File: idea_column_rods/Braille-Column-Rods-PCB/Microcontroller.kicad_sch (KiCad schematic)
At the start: 12 parts, among them J2 Conn_01x02, J3 Conn_01x02, J4 Conn_01x08, SW1 SW_Push, SW2 SW_Push, U3 RP2040-Zero

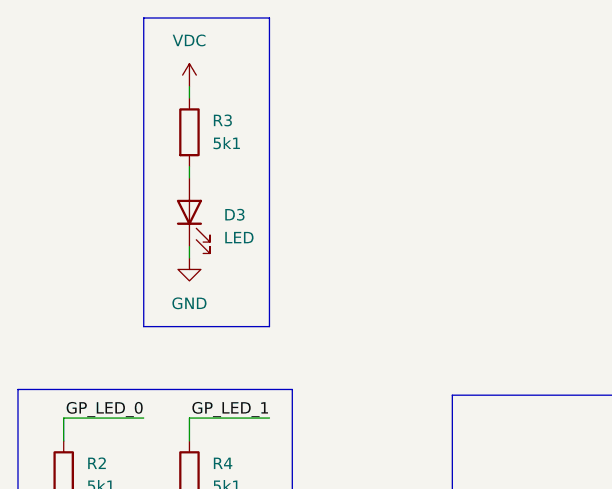
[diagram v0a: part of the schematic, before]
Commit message: WIP: Place the housing and motor X
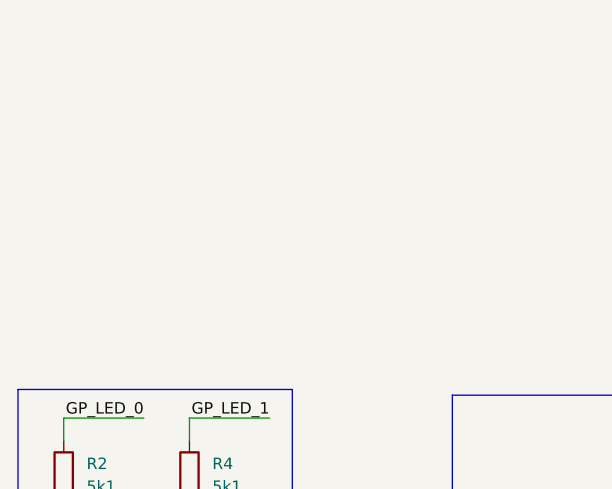
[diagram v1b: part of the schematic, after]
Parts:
- removed D3: LED, LED_SMD:LED_0603_1608Metric_Pad1.05x0.95mm_HandSolder, symbol Device:LED
- removed R3: 5k1, Resistor_SMD:R_0603_1608Metric_Pad0.98x0.95mm_HandSolder, symbol Device:R

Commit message: WIP: Manual routing and silkscreens
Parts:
- removed J2: Conn_01x02, Connector_PinHeader_2.54mm:PinHeader_1x02_P2.54mm_Vertical, symbol Connector_Generic:Conn_01x02
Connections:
- net I2C_SCL: now reaches U3.8 (GP15)
- net I2C_SDA: now reaches U3.9 (GP14)
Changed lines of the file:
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@@
+		)
+	)
+	(global_label "I2C_SDA"
+		(shape input)
+		(at 86.36 91.44 180)
+		(fields_autoplaced yes)
+		(effects
+			(font
+				(size 1.27 1.27)
+			)
+			(justify right)
+		)
+		(property "Intersheetrefs" "${INTERSHEET_REFS}"
+			(at 75.7548 91.44 0)
+			(effects
+				(font
+					(size 1.27 1.27)
+				)
+				(justify right)
+				(hide yes)
+			)
+		)
+	)
+	(global_label "I2C_SCL"
+		(shape input)
+		(at 86.36 88.9 180)
+		(fields_autoplaced yes)
+		(effects
+			(font
+				(size 1.27 1.27)
+			)
+			(justify right)
+		)
+		(property "Intersheetrefs" "${INTERSHEET_REFS}"
+			(at 75.8153 88.9 0)
+			(effects
+				(font
+					(size 1.27 1.27)
+				)
+				(justify right)
+				(hide yes)
+			)
 		)
 	)
@@
 					(unit 1)
 				)
-			)
-		)
-	)
-	(symbol
-		(lib_id "Connector_Generic:Conn_01x02")
-		(at 81.28 88.9 0)
-		(mirror y)
-		(unit 1)
-		(exclude_from_sim no)
-		(in_bom yes)
-		(on_board yes)
-		(dnp no)
-		(property "Reference" "J2"
-			(at 78.994 90.17 90)
-			(effects
-				(font
-					(size 1.27 1.27)
-				)
-			)
-		)
-		(property "Value" "Conn_01x02"
-			(at 81.28 85.09 0)
-			(effects
-				(font
-					(size 1.27 1.27)
-				)
-				(hide yes)
-			)
-		)
-		(property "Footprint" "Connector_PinHeader_2.54mm:PinHeader_1x02_P2.54mm_Vertical"
-			(at 81.28 88.9 0)
-			(effects
-				(font
-					(size 1.27 1.27)
-				)
-				(hide yes)
-			)
-		)
-		(property "Datasheet" "~"
-			(at 81.28 88.9 0)
-			(effects
-				(font
-					(size 1.27 1.27)
-				)
-				(hide yes)
-			)
-		)
-		(property "Description" "Generic connector, single row, 01x02, script generated (kicad-library-utils/schlib/autogen/connector/)"
-			(at 81.28 88.9 0)
-			(effects
-				(font
-					(size 1.27 1.27)
-				)
-				(hide yes)
-			)
-		)
-		(pin "2"
-		)
-		(pin "1"
-		)
-		(instances
-			(project ""
-				(path "/f7fdfeea-4cd4-4338-ad68-f9089a17ed6f/f44c903d-2365-4758-aca6-5117133a8846"
-					(reference "J2")
-					(unit 1)
-				)

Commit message: Complete type 4 rev 1
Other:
- title: (none) -> Braille Cam Rod Prototype (Type 4)
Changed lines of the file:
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@@
 	(generator_version "8.0")
 	(paper "USLetter")
+	(title_block
+		(title "Braille Cam Rod Prototype (Type 4)")
+		(date "2025-01-06")
+		(rev "Rev 1")
+	)
 	(no_connect
 		(at 111.76 139.7)
